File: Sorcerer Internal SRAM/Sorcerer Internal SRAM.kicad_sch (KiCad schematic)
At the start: 13 parts

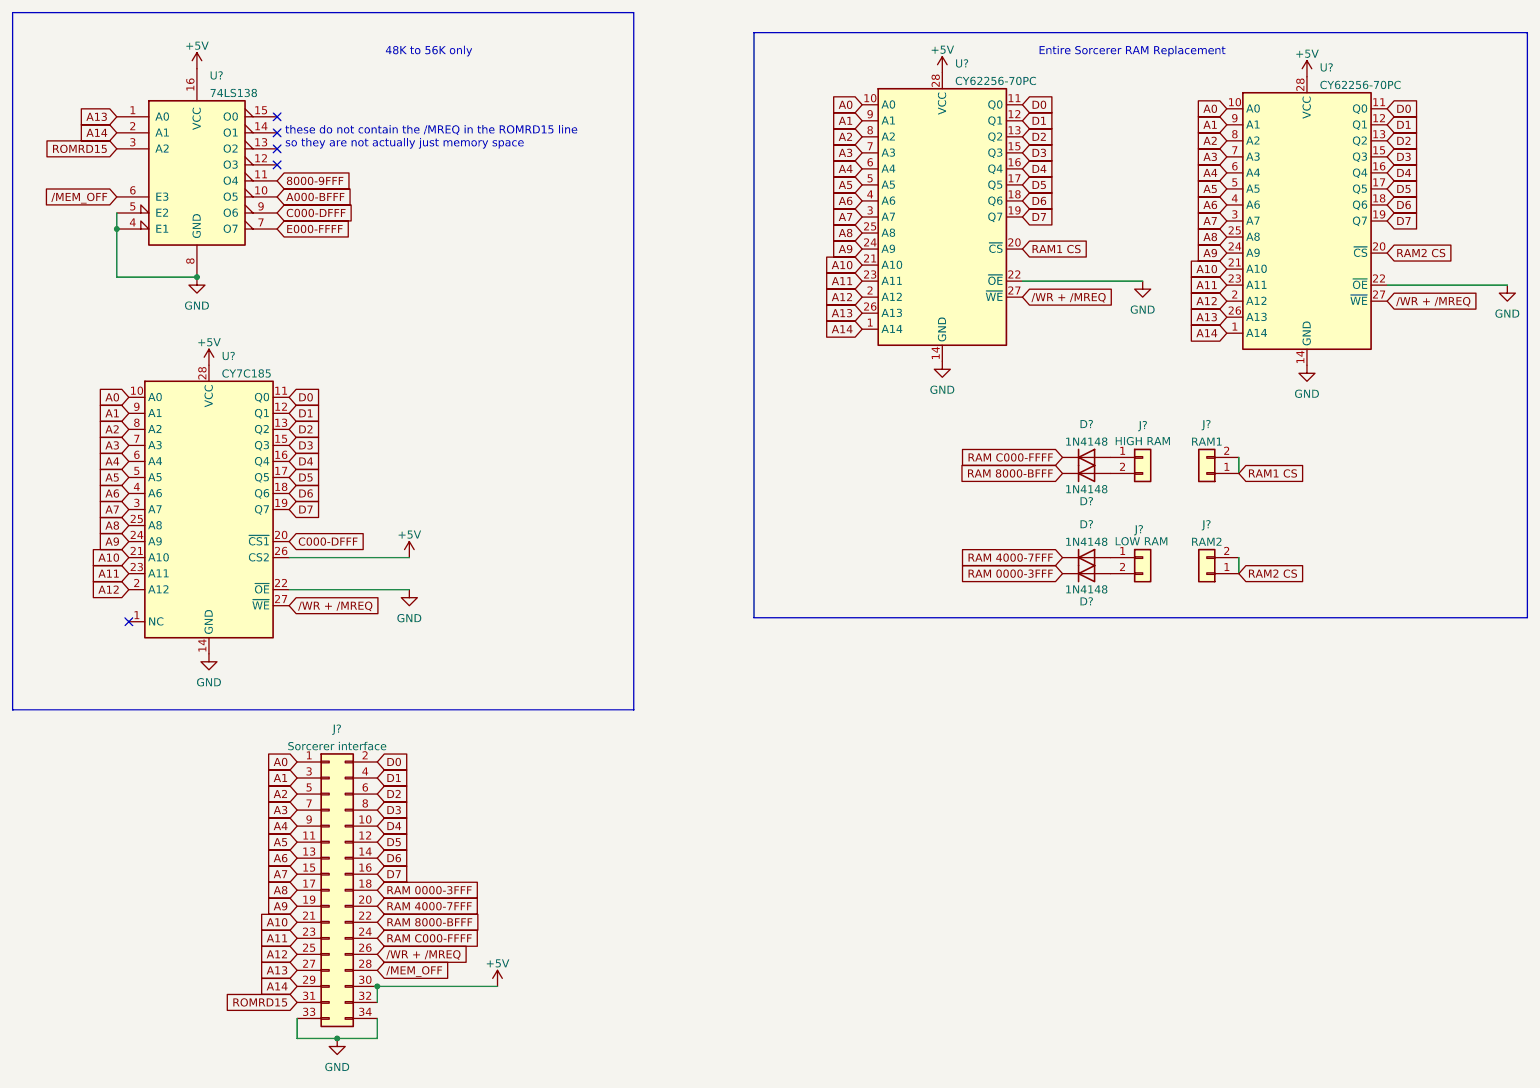
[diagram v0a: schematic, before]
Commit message: laid out SRAM board
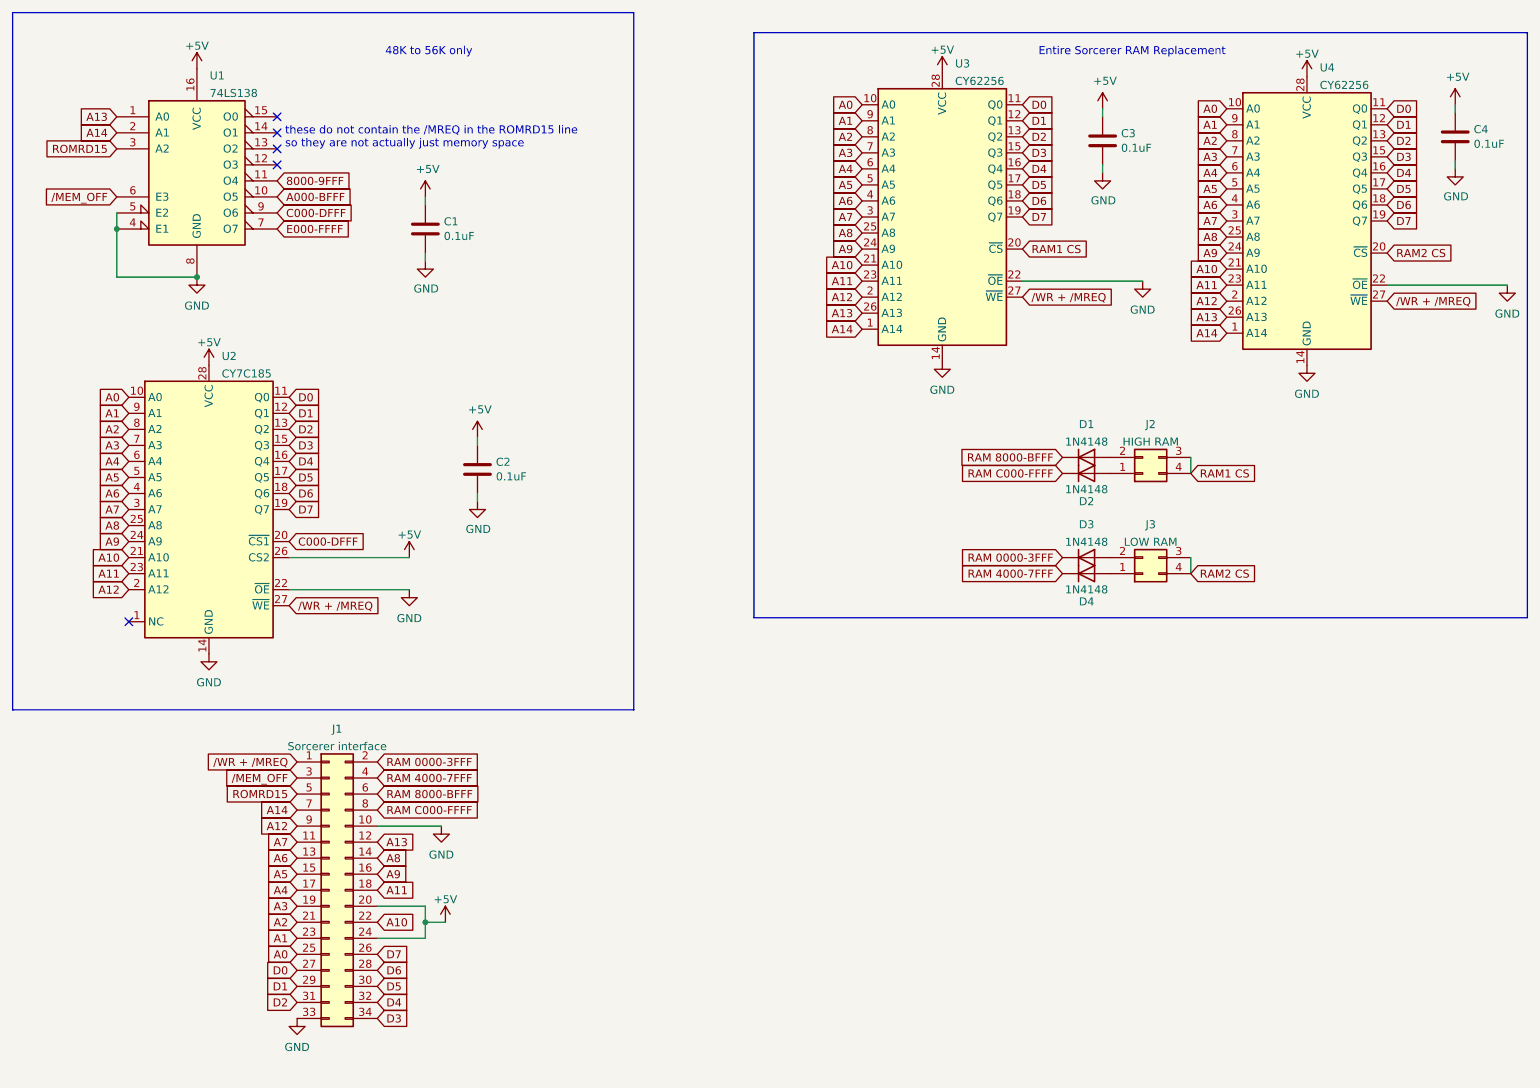
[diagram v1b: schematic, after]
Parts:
- removed J?: RAM2, symbol Connector_Generic:Conn_01x02
- removed J?: HIGH RAM, symbol Connector_Generic:Conn_01x02
- removed J?: LOW RAM, symbol Connector_Generic:Conn_01x02
- removed J?: RAM1, symbol Connector_Generic:Conn_01x02
- added C1, C2, C3, C4: 0.1uF, Capacitor_THT:C_Axial_L3.8mm_D2.6mm_P7.50mm_Horizontal, symbol Device:C
- added J2: HIGH RAM, Connector_PinHeader_2.54mm:PinHeader_2x02_P2.54mm_Vertical, symbol Connector_Generic:Conn_02x02_Counter_Clockwise
- added J3: LOW RAM, Connector_PinHeader_2.54mm:PinHeader_2x02_P2.54mm_Vertical, symbol Connector_Generic:Conn_02x02_Counter_Clockwise
- D1, D2, D3, D4: renamed from D?; footprint Diode_THT:D_DO-35_SOD27_P7.62mm_Horizontal -> Diode_THT:D_DO-35_SOD27_P2.54mm_Vertical_KathodeUp
- J1: renamed from J?; footprint (none) -> Connector_PinHeader_2.54mm:PinHeader_2x17_P2.54mm_Vertical
- U1: renamed from U?; footprint (none) -> Package_DIP:DIP-16_W7.62mm
- U3, U4: renamed from U?; value CY62256-70PC -> CY62256
- gave numbers to parts that had none: 1
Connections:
- net +5V: now also J1.20 (Pin_20), J1.24 (Pin_24), C1.1, C2.1, C3.1, C4.1; no longer J1.30 (Pin_30), J1.32 (Pin_32)
- net A0: now also J1.25 (Pin_25); no longer J1.1 (Pin_1)
- net A1: now also J1.23 (Pin_23); no longer J1.3 (Pin_3)
- net A10: now also J1.22 (Pin_22); no longer J1.21 (Pin_21)
- net A11: now also J1.18 (Pin_18); no longer J1.23 (Pin_23)
- net A12: now also J1.9 (Pin_9); no longer J1.25 (Pin_25)
- net A13: now also J1.12 (Pin_12); no longer J1.27 (Pin_27)
- net A14: now also J1.7 (Pin_7); no longer J1.29 (Pin_29)
- net A2: now also J1.21 (Pin_21); no longer J1.5 (Pin_5)
- net A3: now also J1.19 (Pin_19); no longer J1.7 (Pin_7)
- net A4: now also J1.17 (Pin_17); no longer J1.9 (Pin_9)
- net A5: now also J1.15 (Pin_15); no longer J1.11 (Pin_11)
- net A7: now also J1.11 (Pin_11); no longer J1.15 (Pin_15)
- net A8: now also J1.14 (Pin_14); no longer J1.17 (Pin_17)
- net A9: now also J1.16 (Pin_16); no longer J1.19 (Pin_19)
- net D0: now also J1.27 (Pin_27); no longer J1.2 (Pin_2)
- net D1: now also J1.29 (Pin_29); no longer J1.4 (Pin_4)
- net D2: now also J1.31 (Pin_31); no longer J1.6 (Pin_6)
- net D3: now also J1.34 (Pin_34); no longer J1.8 (Pin_8)
- net D4: now also J1.32 (Pin_32); no longer J1.10 (Pin_10)
- net D5: now also J1.30 (Pin_30); no longer J1.12 (Pin_12)
- net D6: now also J1.28 (Pin_28); no longer J1.14 (Pin_14)
- net D7: now also J1.26 (Pin_26); no longer J1.16 (Pin_16)
- net GND: now also J1.10 (Pin_10), C1.2, C2.2, C3.2, C4.2; no longer J1.34 (Pin_34)
- net RAM 0000-3FFF: now also D3.1 (K), J1.2 (Pin_2); no longer D4.1 (K), J1.18 (Pin_18)
- net RAM 4000-7FFF: now also D4.1 (K), J1.4 (Pin_4); no longer D3.1 (K), J1.20 (Pin_20)
- net RAM 8000-BFFF: now also D1.1 (K), J1.6 (Pin_6); no longer D2.1 (K), J1.22 (Pin_22)
- net RAM C000-FFFF: now also D2.1 (K), J1.8 (Pin_8); no longer D1.1 (K), J1.24 (Pin_24)
- net RAM1 CS: now also J2.3 (Pin_3), J2.4 (Pin_4)
- net RAM2 CS: now also J3.3 (Pin_3), J3.4 (Pin_4)
- net ROMRD15: now also J1.5 (Pin_5); no longer J1.31 (Pin_31)
- net /MEM_OFF: now also J1.3 (Pin_3); no longer J1.28 (Pin_28)
- net /WR + /MREQ: now also J1.1 (Pin_1); no longer J1.26 (Pin_26)
- net at D1.2 (A): now also J2.2 (Pin_2)
- net at D2.2 (A): now also J2.1 (Pin_1)
- net at D3.2 (A): now also J3.2 (Pin_2)
- net at D4.2 (A): now also J3.1 (Pin_1)
